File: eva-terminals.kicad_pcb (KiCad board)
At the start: 2 copper layers, 64 x 64 mm, 30 parts, among them J1 691403900006B, J2 691403900006B, J3 Conn_01x04, J4 691403900006B, J5 HEATER, J6 Conn_02x10_Odd_Even, J7 Conn_02x10_Odd_Even, J8 SPI, U1 LD39015M33R, U2 ADXL345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

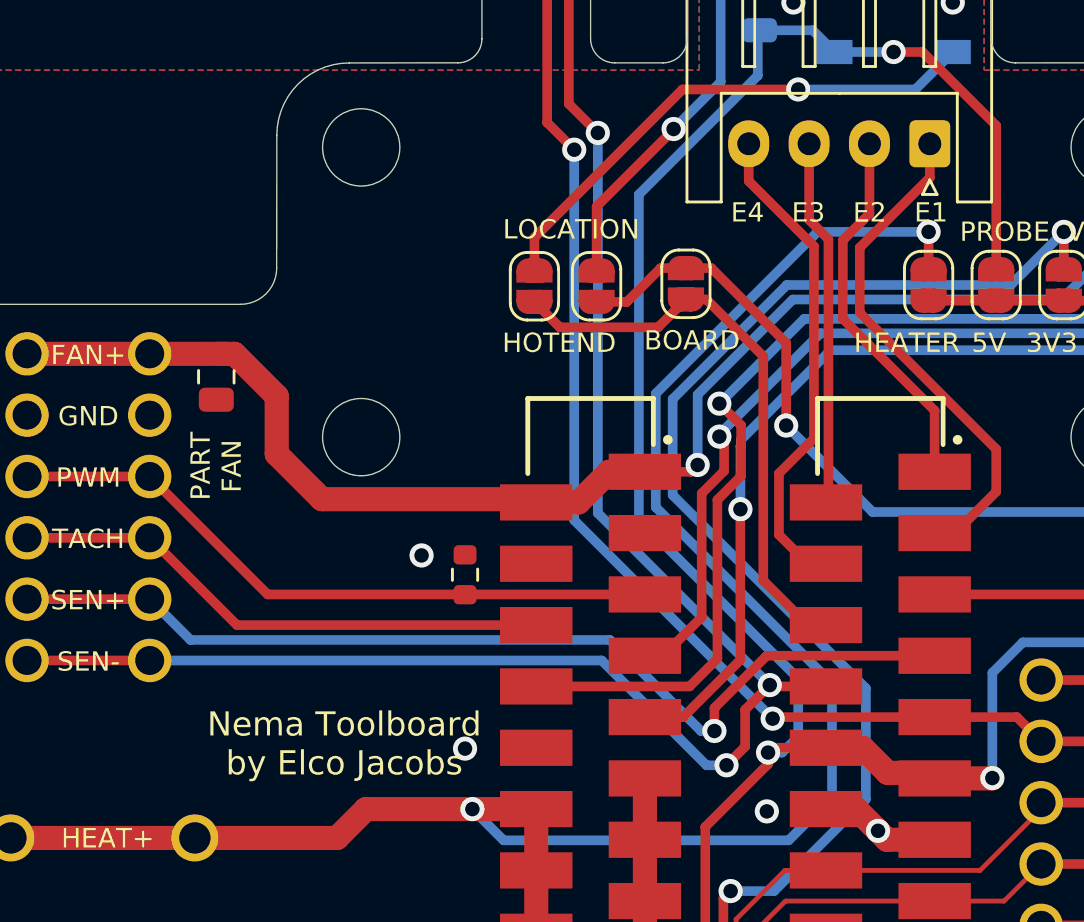
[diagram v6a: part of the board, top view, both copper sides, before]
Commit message: removed unncessary via in groundref
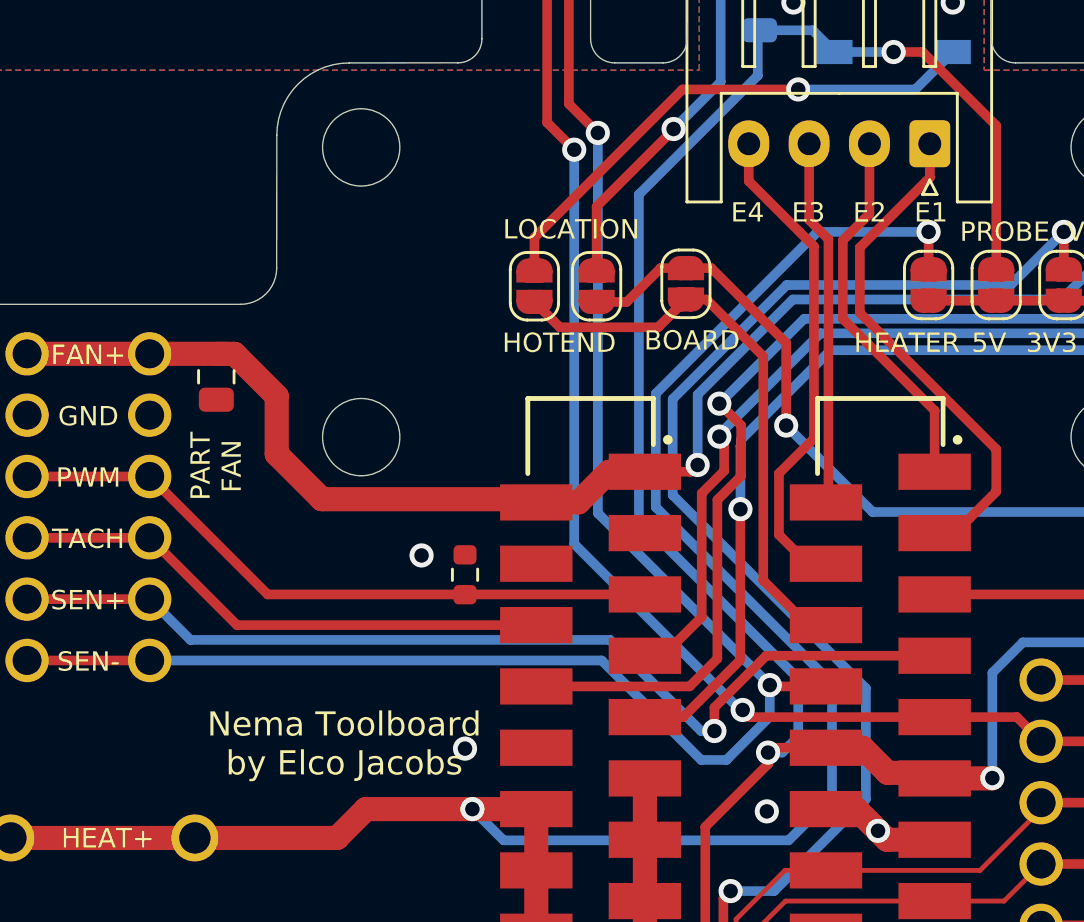
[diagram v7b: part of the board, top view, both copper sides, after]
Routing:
- net CHAMBER_TEMP: track 54.9 -> 55.4 mm
- net GNDREF: track 76.9 -> 76.6 mm, vias 3 -> 2
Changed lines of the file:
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@@
   (segment (start 104.075 110.39) (end 103.75 110.065) (width 0.4) (layer "F.Cu") (net 30))
   (segment (start 129.34 110.39) (end 124.26 110.39) (width 0.4) (layer "F.Cu") (net 30))
-  (segment (start 99.128602 95.719946) (end 99.128602 96.671398) (width 0.4) (layer "F.Cu") (net 31))
-  (segment (start 101.293548 93.555) (end 99.128602 95.719946) (width 0.4) (layer "F.Cu") (net 31))
-  (segment (start 108.25 93.555) (end 101.293548 93.555) (width 0.4) (layer "F.Cu") (net 31))
+  (segment (start 101.272912 93.555) (end 99.128602 95.69931) (width 0.4) (layer "F.Cu") (net 31))
+  (segment (start 108.25 93.555) (end 101.272912 93.555) (width 0.4) (layer "F.Cu") (net 31))
+  (segment (start 99.128602 95.69931) (end 99.128602 96.671398) (width 0.4) (layer "F.Cu") (net 31))
   (segment (start 75.74 91.21) (end 70.66 91.21) (width 0.4) (layer "F.Cu") (net 31))
   (via (at 99.128602 96.671398) (size 1) (drill 0.6) (layers "F.Cu" "B.Cu") (net 31))
@@
   (segment (start 93.1 60.3875) (end 93.1 70.7) (width 0.4) (layer "F.Cu") (net 32))
   (segment (start 93.1 70.7) (end 94.3 71.9) (width 0.4) (layer "F.Cu") (net 32))
-  (segment (start 100.400499 95.790845) (end 101.421715 94.769629) (width 0.4) (layer "F.Cu") (net 32))
-  (segment (start 99.63 98.09) (end 100.400499 97.319501) (width 0.4) (layer "F.Cu") (net 32))
-  (segment (start 100.400499 97.319501) (end 100.400499 95.790845) (width 0.4) (layer "F.Cu") (net 32))
   (segment (start 103.75 94.825) (end 101.477086 94.825) (width 0.4) (layer "F.Cu") (net 32))
   (segment (start 75.74 93.75) (end 70.66 93.75) (width 0.4) (layer "F.Cu") (net 32))
   (via (at 101.421715 94.769629) (size 1) (drill 0.6) (layers "F.Cu" "B.Cu") (net 32))
-  (via (at 99.63 98.09) (size 1) (drill 0.6) (layers "F.Cu" "B.Cu") (net 32))
   (via (at 94.3 71.9) (size 1) (drill 0.6) (layers "F.Cu" "B.Cu") (net 32))
-  (segment (start 94.46 93.75) (end 98.8 98.09) (width 0.4) (layer "B.Cu") (net 32))
-  (segment (start 75.74 93.75) (end 94.46 93.75) (width 0.4) (layer "B.Cu") (net 32))
-  (segment (start 98.8 98.09) (end 99.63 98.09) (width 0.4) (layer "B.Cu") (net 32))
+  (segment (start 101.421715 96.078285) (end 99.63 97.87) (width 0.4) (layer "B.Cu") (net 32))
+  (segment (start 99.63 97.87) (end 98.58 97.87) (width 0.4) (layer "B.Cu") (net 32))
+  (segment (start 98.58 97.87) (end 94.46 93.75) (width 0.4) (layer "B.Cu") (net 32))
+  (segment (start 94.46 93.75) (end 75.74 93.75) (width 0.4) (layer "B.Cu") (net 32))
   (segment (start 101.421715 94.769629) (end 94.3 87.647914) (width 0.4) (layer "B.Cu") (net 32))
   (segment (start 94.3 87.647914) (end 94.3 71.9) (width 0.4) (layer "B.Cu") (net 32))
+  (segment (start 101.421715 94.769629) (end 101.421715 96.078285) (width 0.4) (layer "B.Cu") (net 32))
   (segment (start 97.805826 70.1) (end 102.6 70.1) (width 0.4) (layer "F.Cu") (net 33))
   (segment (start 91.675 76.230826) (end 97.805826 70.1) (width 0.4) (layer "F.Cu") (net 33))
@@
   (segment (start 109 68.55) (end 107.45 70.1) (width 0.4) (layer "B.Cu") (net 33))
   (segment (start 107.45 70.1) (end 102.6 70.1) (width 0.4) (layer "B.Cu") (net 33))
-  (segment (start 101.605 96.095) (end 101.54 96.16) (width 0.4) (layer "F.Cu") (net 34))
   (segment (start 92.2 71.472806) (end 93.32277 72.595576) (width 0.4) (layer "F.Cu") (net 34))
   (segment (start 111.655 96.095) (end 112.66 97.1) (width 0.4) (layer "F.Cu") (net 34))
-  (segment (start 108.25 96.095) (end 101.605 96.095) (width 0.4) (layer "F.Cu") (net 34))
+  (segment (start 108.25 96.095) (end 100.595 96.095) (width 0.4) (layer "F.Cu") (net 34))
   (segment (start 112.66 97.1) (end 117.74 97.1) (width 0.4) (layer "F.Cu") (net 34))
   (segment (start 92.2 62.4125) (end 92.2 71.472806) (width 0.4) (layer "F.Cu") (net 34))
+  (segment (start 100.595 96.095) (end 100.3 95.8) (width 0.4) (layer "F.Cu") (net 34))
   (segment (start 91.75 61.9625) (end 92.2 62.4125) (width 0.4) (layer "F.Cu") (net 34))
   (segment (start 108.25 96.095) (end 111.655 96.095) (width 0.4) (layer "F.Cu") (net 34))
   (via (at 93.32277 72.595576) (size 1) (drill 0.6) (layers "F.Cu" "B.Cu") (net 34))
-  (via (at 101.54 96.16) (size 1) (drill 0.6) (layers "F.Cu" "B.Cu") (net 34))
-  (segment (start 93.32277 87.94277) (end 93.32277 72.595576) (width 0.4) (layer "B.Cu") (net 34))
-  (segment (start 101.54 96.16) (end 93.32277 87.94277) (width 0.4) (layer "B.Cu") (net 34))
+  (via (at 100.3 95.8) (size 1) (drill 0.6) (layers "F.Cu" "B.Cu") (net 34))
+  (segment (start 93.32277 72.595576) (end 93.32277 88.92277) (width 0.4) (layer "B.Cu") (net 34))
+  (segment (start 93.32277 88.92277) (end 100.2 95.8) (width 0.4) (layer "B.Cu") (net 34))
+  (segment (start 100.2 95.8) (end 100.3 95.8) (width 0.4) (layer "B.Cu") (net 34))
   (segment (start 119.15 77.55) (end 120.7 77.55) (width 0.4) (layer "F.Cu") (net 35))
   (segment (start 120.7 77.55) (end 122 78.85) (width 0.4) (layer "F.Cu") (net 35))

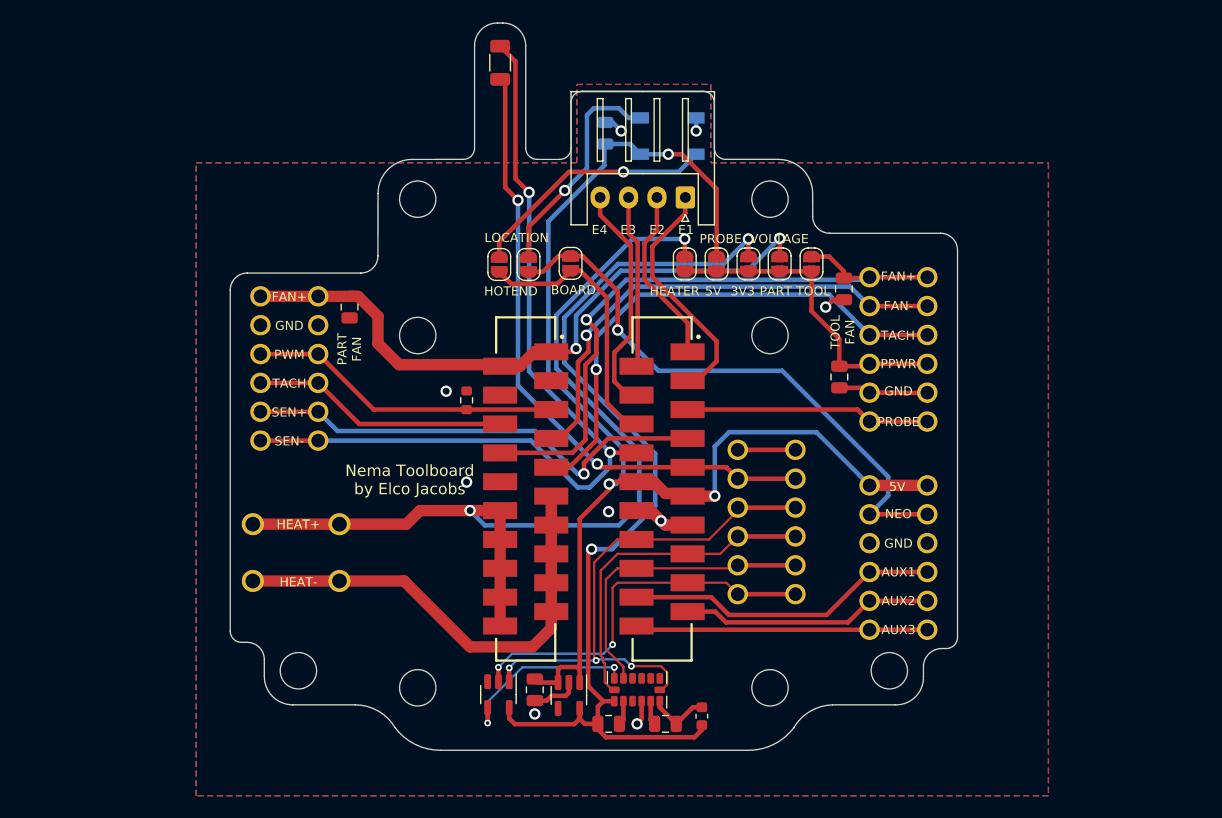
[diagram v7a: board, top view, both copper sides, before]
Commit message: add fiducial
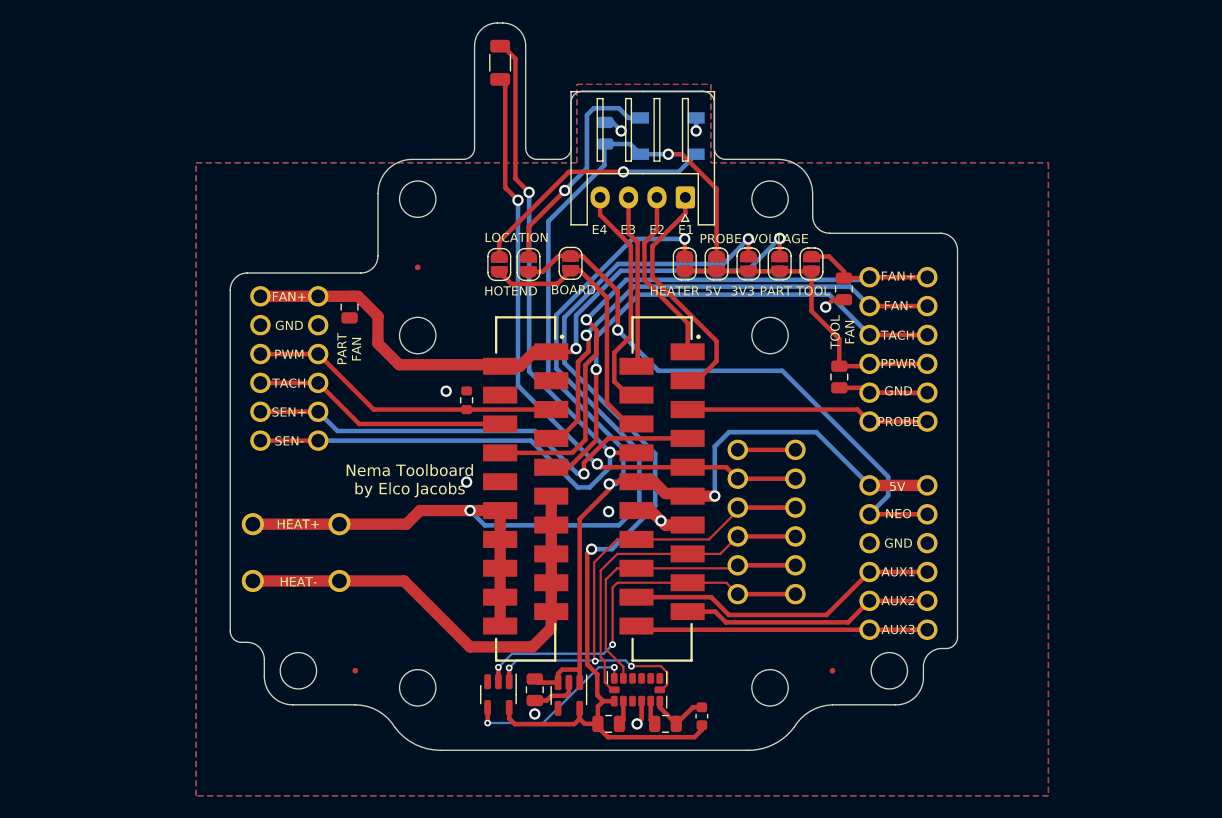
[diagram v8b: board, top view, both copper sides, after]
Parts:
- added REF**: Fiducial_0.5mm_Mask1.5mm, Fiducial:Fiducial_0.5mm_Mask1.5mm, F.Cu at (121.0, 114.0)
- added REF**: Fiducial_0.5mm_Mask1.5mm, Fiducial:Fiducial_0.5mm_Mask1.5mm, F.Cu at (79.0, 114.0)
- added REF**: Fiducial_0.5mm_Mask1.5mm, Fiducial:Fiducial_0.5mm_Mask1.5mm, F.Cu at (84.5, 78.5)
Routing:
- net Net-(U2-Pad13): track 16.6 -> 15.5 mm
